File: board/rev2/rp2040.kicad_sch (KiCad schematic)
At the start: 36 parts, among them U8 TLV74311, U9 RP2354B, Y1 ABM8-272-T3

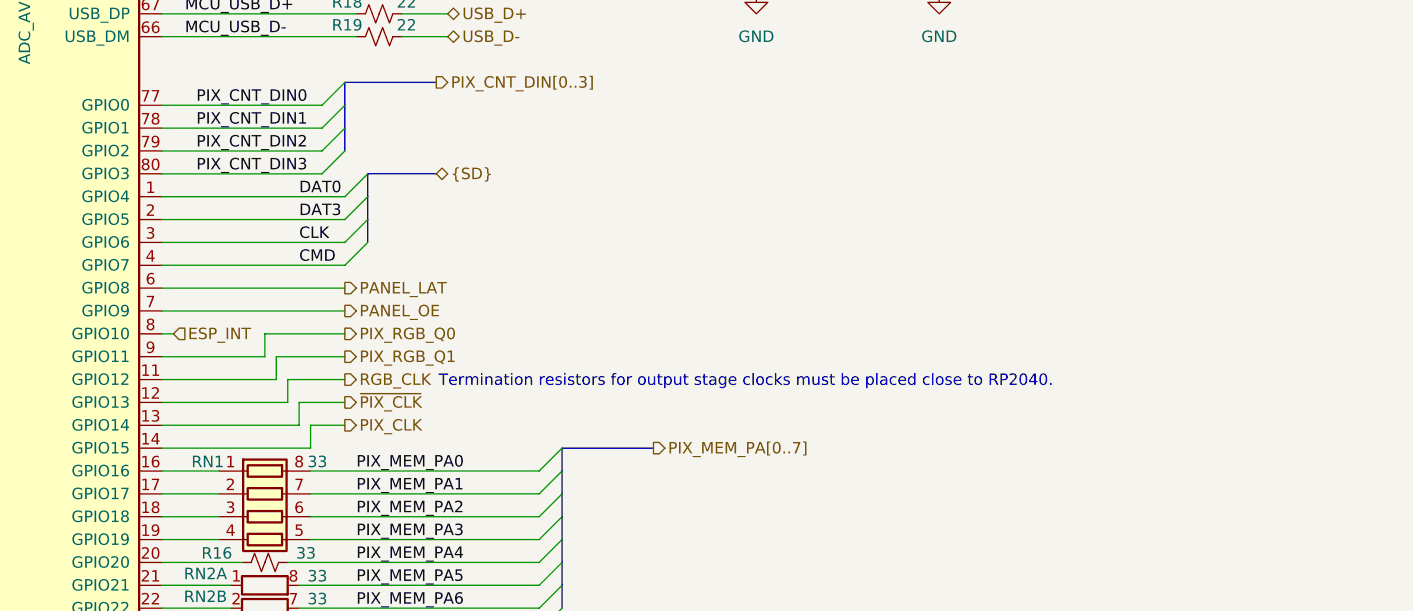
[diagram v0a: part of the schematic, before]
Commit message: More tweaks to schematic, start laying out regulators
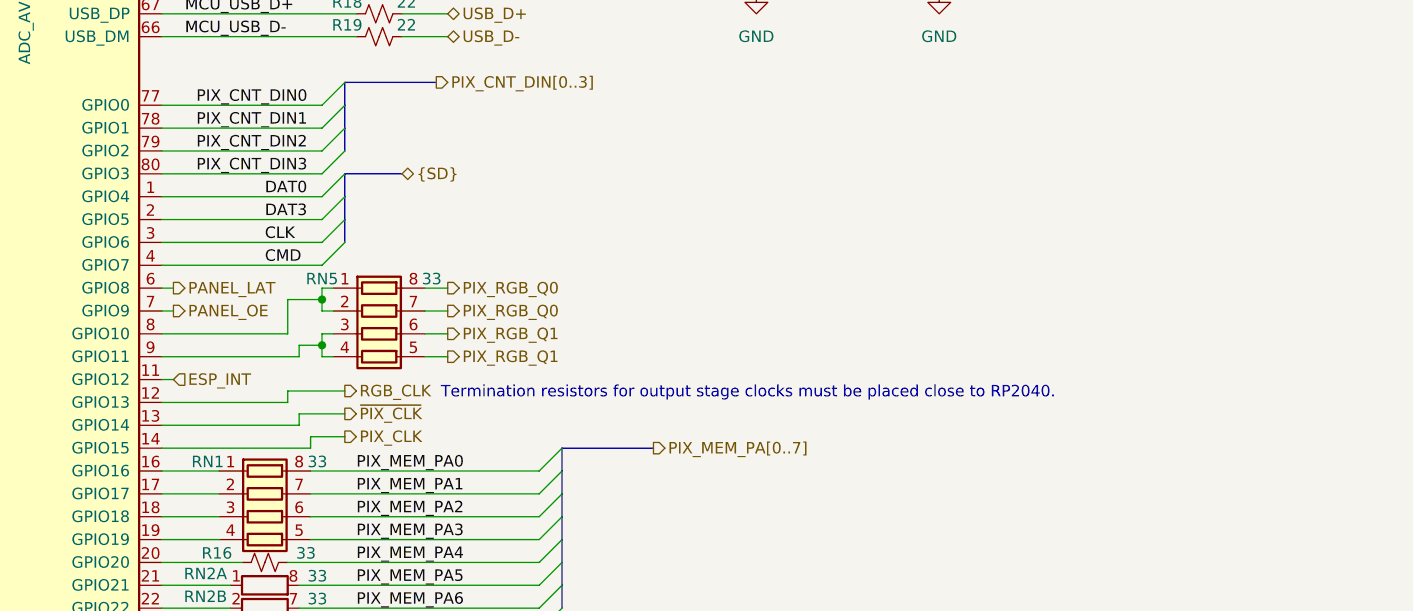
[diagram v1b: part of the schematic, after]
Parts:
- added RN5: 33, RN_SMD:R_Array_Flat_4x0201, symbol Device:R_Pack04
- R20, R21: footprint Resistor_SMD:R_0805_2012Metric -> Resistor_SMD:R_0402_1005Metric; LCSC C17414 -> C25744; Part 0805W8F1002T5E -> 0402WGF1002TCE
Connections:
- net ESP_INT: now also U9.11 (GPIO12); no longer U9.8 (GPIO10)
- net PIX_RGB_Q0: now also RN5.7 (R2.2), RN5.8 (R1.2); no longer U9.9 (GPIO11)
- net PIX_RGB_Q1: now also RN5.5 (R4.2), RN5.6 (R3.2); no longer U9.11 (GPIO12)
- new net: RN5.1 (R1.1), RN5.2 (R2.1), U9.8 (GPIO10)
- new net: RN5.3 (R3.1), RN5.4 (R4.1), U9.9 (GPIO11)

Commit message: 3.3V LDO
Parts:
- removed RN1, RN3, RN4, RN5: 33, RN_SMD:R_Array_Flat_4x0201, symbol Device:R_Pack04
- removed RN2: 33, RN_SMD:R_Array_Flat_4x0201, symbol Device:R_Pack04_Split
- added R22, R23, R49, R50, R51: 33, Resistor_SMD:R_0402_1005Metric, symbol Device:R_Small_US
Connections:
- net ESP_INT: now also U9.12 (GPIO13); no longer U9.11 (GPIO12)
- net PIX_MEM_PA0: now also U9.16 (GPIO16)
- net PIX_MEM_PA1: now also U9.17 (GPIO17)
- net PIX_MEM_PA2: now also U9.18 (GPIO18)
- net PIX_MEM_PA3: now also U9.19 (GPIO19)
- net PIX_MEM_PA4: now also U9.20 (GPIO20); no longer R16.2
- net PIX_MEM_PA5: now also U9.21 (GPIO21)
- net PIX_MEM_PA6: now also U9.22 (GPIO22)
- net PIX_MEM_PA7: now also U9.23 (GPIO23)
- net PIX_MEM_PB0: now also U9.25 (GPIO24)
- net PIX_MEM_PB1: now also U9.26 (GPIO25)
- net PIX_MEM_PB2: now also U9.27 (GPIO26)
- net PIX_MEM_PB3: now also U9.28 (GPIO27)
- net PIX_MEM_PB4: now also U9.36 (GPIO28)
- net PIX_MEM_PB5: now also U9.37 (GPIO29)
- net PIX_MEM_PB6: now also U9.38 (GPIO30)
- net PIX_MEM_PB7: now also U9.39 (GPIO31)
- net PIX_RGB_Q0: now also R16.2, R22.2
- net PIX_RGB_Q1: now also R23.2, R49.2
- net RGB_CLK: now also R50.2, R51.2; no longer U9.12 (GPIO13)
- net at R16.1: now also U9.8 (GPIO10), R22.1; no longer U9.20 (GPIO20)
- net at U9.9 (GPIO11): now also R23.1, R49.1
- new net: R50.1, R51.1, U9.11 (GPIO12)
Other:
- note removed: "Termination resistors for output stage clocks must be placed close to RP2040."

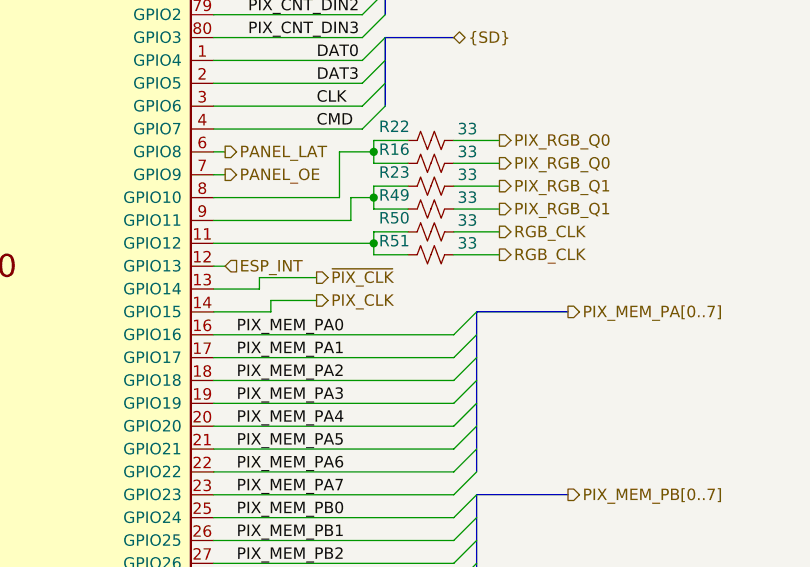
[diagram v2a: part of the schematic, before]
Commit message: Layout more component blocks
- regulators
- mcus

Still need to do the decoders + overall packing
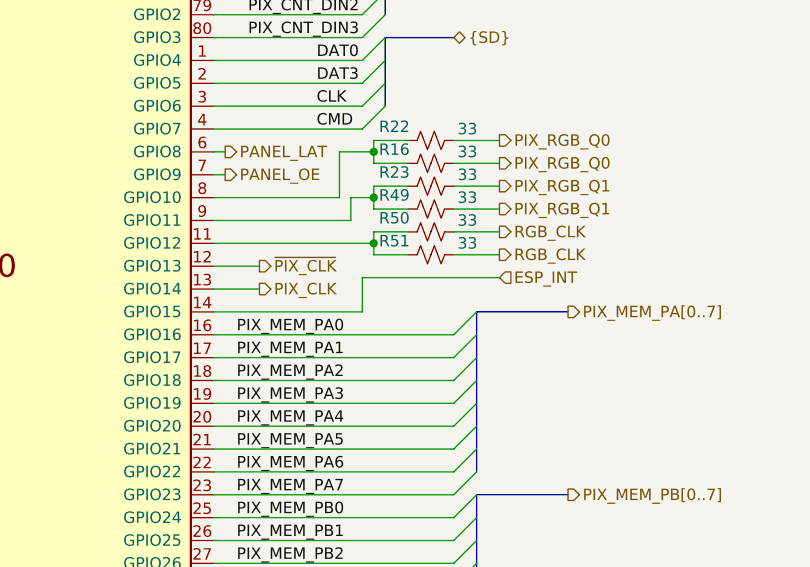
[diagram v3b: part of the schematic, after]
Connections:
- net ESP_INT: now also U9.14 (GPIO15); no longer U9.12 (GPIO13)
- net PIX_CLK: now also U9.13 (GPIO14); no longer U9.14 (GPIO15)
- net ~{PIX_CLK}: now also U9.12 (GPIO13); no longer U9.13 (GPIO14)
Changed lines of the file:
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@@
-	(wire
-		(pts
-			(xy 138.43 95.25) (xy 138.43 96.52)
-		)
-		(stroke
-			(width 0)
-			(type default)
-		)
-	)
 	(wire
 		(pts
@@
 		)
 	)
+	(wire
+		(pts
+			(xy 148.59 92.71) (xy 148.59 96.52)
+		)
+		(stroke
+			(width 0)
+			(type default)
+		)
+	)
 	(bus
 		(pts
@@
 	(wire
 		(pts
-			(xy 132.08 96.52) (xy 138.43 96.52)
-		)
-		(stroke
-			(width 0)
-			(type default)
-		)
-	)
-	(wire
-		(pts
 			(xy 205.74 153.67) (xy 205.74 157.48)
 		)
@@
 		)
 	)
-	(wire
-		(pts
-			(xy 133.35 91.44) (xy 132.08 91.44)
-		)
-		(stroke
-			(width 0)
-			(type default)
-		)
-	)
 	(bus
 		(pts
@@
 	(wire
 		(pts
-			(xy 132.08 93.98) (xy 137.16 93.98)
-		)
-		(stroke
-			(width 0)
-			(type default)
-		)
-	)
-	(wire
-		(pts
 			(xy 48.26 101.6) (xy 48.26 107.95)
 		)
@@
 		)
 	)
+	(wire
+		(pts
+			(xy 137.16 91.44) (xy 132.08 91.44)
+		)
+		(stroke
+			(width 0)
+			(type default)
+		)
+	)
 	(bus
 		(pts
@@
 	(wire
 		(pts
+			(xy 148.59 96.52) (xy 132.08 96.52)
+		)
+		(stroke
+			(width 0)
+			(type default)
+		)
+	)
+	(wire
+		(pts
+			(xy 137.16 93.98) (xy 132.08 93.98)
+		)
+		(stroke
+			(width 0)
+			(type default)
+		)
+	)
+	(wire
+		(pts
 			(xy 99.06 38.1) (xy 99.06 40.64)
 		)
@@
 	(wire
 		(pts
-			(xy 137.16 92.71) (xy 143.51 92.71)
-		)
-		(stroke
-			(width 0)
-			(type default)
-		)
-	)
-	(wire
-		(pts
 			(xy 132.08 137.16) (xy 158.75 137.16)
 		)
@@
 		)
 	)
-	(wire
-		(pts
-			(xy 138.43 95.25) (xy 143.51 95.25)
-		)
-		(stroke
-			(width 0)
-			(type default)
-		)
-	)
 	(bus
 		(pts
@@
 	(wire
 		(pts
-			(xy 137.16 92.71) (xy 137.16 93.98)
-		)
-		(stroke
-			(width 0)
-			(type default)
-		)
-	)
-	(wire
-		(pts
 			(xy 138.43 142.24) (xy 132.08 142.24)
 		)
@@
 		(pts
 			(xy 132.08 165.1) (xy 144.78 165.1)
+		)
+		(stroke
+			(width 0)
+			(type default)
+		)
+	)
+	(wire
+		(pts
+			(xy 163.83 92.71) (xy 148.59 92.71)
 		)
 		(stroke
@@
 		)
 	)
-	(hierarchical_label "ESP_INT"
-		(shape input)
-		(at 133.35 91.44 0)
-		(effects
-			(font
-				(size 1.27 1.27)
-			)
-			(justify left)
-		)
-	)
 	(hierarchical_label "PIX_RGB_Q1"
 		(shape output)
@@
 	(hierarchical_label "~{PIX_CLK}"
 		(shape output)
-		(at 143.51 92.71 0)
+		(at 137.16 91.44 0)
 		(effects
 			(font
@@
 		)
 	)
+	(hierarchical_label "ESP_INT"
+		(shape input)
+		(at 163.83 92.71 0)
+		(effects
+			(font
+				(size 1.27 1.27)
+			)
+			(justify left)
+		)
+	)
 	(hierarchical_label "PIX_CLK"
 		(shape output)
-		(at 143.51 95.25 0)
-		(effects
-			(font
+		(at 137.16 93.98 0)
+		(effects
+			(font

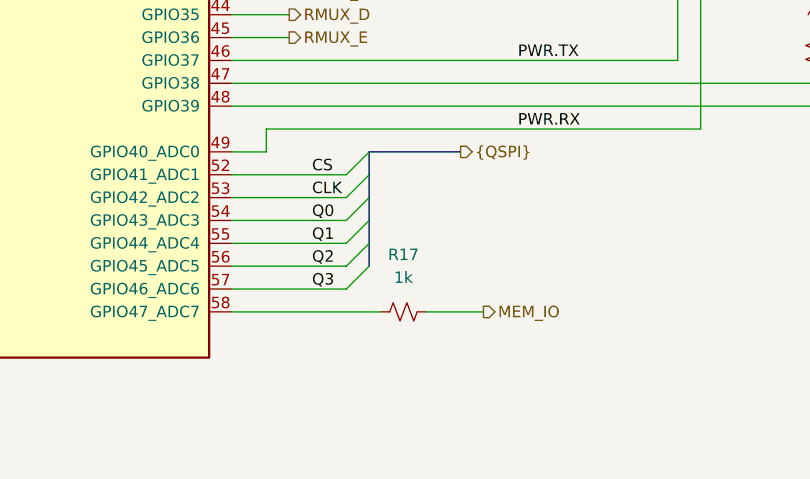
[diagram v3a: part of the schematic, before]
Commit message: Rough full board layout
also, start re-organizing which pins of buffers/gates are used for what

still need to reorder the mem i/o lines to align better

also fix duplicate pullups and fix mem_io isolation res
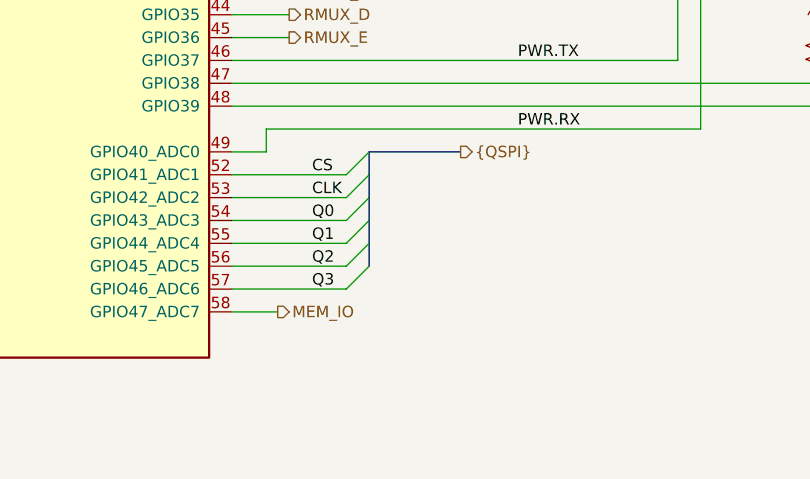
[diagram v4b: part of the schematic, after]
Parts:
- removed R17: 1k, Resistor_SMD:R_0402_1005Metric, symbol Device:R_Small_US
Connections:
- net MEM_IO: now also U9.58 (GPIO47_ADC7)
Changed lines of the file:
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@@
 	(wire
 		(pts
-			(xy 132.08 180.34) (xy 148.59 180.34)
+			(xy 132.08 180.34) (xy 137.16 180.34)
 		)
 		(stroke
@@
 	(wire
 		(pts
-			(xy 153.67 180.34) (xy 160.02 180.34)
-		)
-		(stroke
-			(width 0)
-			(type default)
-		)
-	)
-	(wire
-		(pts
 			(xy 85.09 40.64) (xy 85.09 38.1)
 		)
@@
 	(hierarchical_label "MEM_IO"
 		(shape output)
-		(at 160.02 180.34 0)
+		(at 137.16 180.34 0)
 		(effects
 			(font
@@
 					(unit 1)
 				)
-			)
-		)
-	)
-	(symbol
-		(lib_id "Device:R_Small_US")
-		(at 151.13 180.34 90)
-		(unit 1)
-		(exclude_from_sim no)
-		(in_bom yes)
-		(on_board yes)
-		(dnp no)
-		(fields_autoplaced yes)
-		(property "Reference" "R17"
-			(at 151.13 173.99 90)
-			(effects
-				(font
-					(size 1.27 1.27)
-				)
-			)
-		)
-		(property "Value" "1k"
-			(at 151.13 176.53 90)
-			(effects
-				(font
-					(size 1.27 1.27)
-				)
-			)
-		)
-		(property "Footprint" "Resistor_SMD:R_0402_1005Metric"
-			(at 151.13 180.34 0)
-			(effects
-				(font
-					(size 1.27 1.27)
-				)
-				(hide yes)
-			)
-		)
-		(property "Datasheet" "~"
-			(at 151.13 180.34 0)
-			(effects
-				(font
-					(size 1.27 1.27)
-				)
-				(hide yes)
-			)
-		)
-		(property "Description" "Resistor, small US symbol"
-			(at 151.13 180.34 0)
-			(effects
-				(font
-					(size 1.27 1.27)
-				)
-				(hide yes)
-			)
-		)
-		(property "Part" "0402WGF1001TCE"
-			(at 151.13 180.34 90)
-			(effects
-				(font
-					(size 1.27 1.27)
-				)
-				(hide yes)
-			)
-		)
-		(property "LCSC" "C11702"
-			(at 151.13 180.34 90)
-			(effects
-				(font
-					(size 1.27 1.27)
-				)
-				(hide yes)
-			)
-		)
-		(pin "2"
-		)
-		(pin "1"
-		)
-		(instances
-			(project "mainboard"
-				(path "/32eb05c7-b4a6-42f3-8fb3-43453631100f/09159769-9a8d-41b9-89ab-3a0a86692893"
-					(reference "R17")
-					(unit 1)
-				)

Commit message: Finish board rev2
woo another pcb
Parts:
- added TP6: TestPoint, TestPoint:TestPoint_Pad_D1.0mm, symbol Connector:TestPoint
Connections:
- net CLK: no longer U9.3 (GPIO6)
- net DVDD: now also TP6.1
- net PIX_MEM_PA0: now also U9.18 (GPIO18); no longer U9.16 (GPIO16)
- net PIX_MEM_PA2: now also U9.16 (GPIO16); no longer U9.18 (GPIO18)
- new net SDCLK: U9.3 (GPIO6)
